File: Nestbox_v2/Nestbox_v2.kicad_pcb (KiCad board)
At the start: 2 copper layers, 85 x 60 mm, 116 parts, among them CON301 Micro_SD_Card, J201 BATT_CONN_01X02, J401 LB_DETECT_CONN_01X04, J402 CONN_01X05, J501 CONN_01X01, J502 CONN_01X06, J601 LOAD_CELL_CONN_01X04, J701 RFID_CONN_01X05, P301 RX/TX, P302 TST/RST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

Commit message: second PCB for EM4095 and created fabrication files of main board and corrected holes locations
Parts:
- moved C201 189.3 mm to (73.7, -20.5)
- moved C202 189.3 mm to (-3.31, -22.5)
- moved C203 189.3 mm to (63.5, -40.5)
- moved C204 189.3 mm to (-3.31, -14.5)
- moved C205 189.3 mm to (66.7, -20.5)
- moved C206 189.3 mm to (59.5, -41.0)
- moved C207 189.3 mm to (61.5, -41.0)
- moved C208 189.3 mm to (67.0, -38.0)
- moved C209 189.3 mm to (68.0, -41.0)
- moved C210 189.3 mm to (73.0, -41.0)
- moved C301 189.3 mm to (55.0, -23.0)
- moved C302 189.3 mm to (58.2, -20.0)
- moved C303 189.3 mm to (58.2, -18.0)
- moved C304 189.3 mm to (55.5, -12.0)
- moved C305 189.3 mm to (55.5, -13.7)
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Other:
- board text added: "VDD DATA CLK SLEEP GND"
- board text removed: "VDD CLK DATA SLEEP GND"

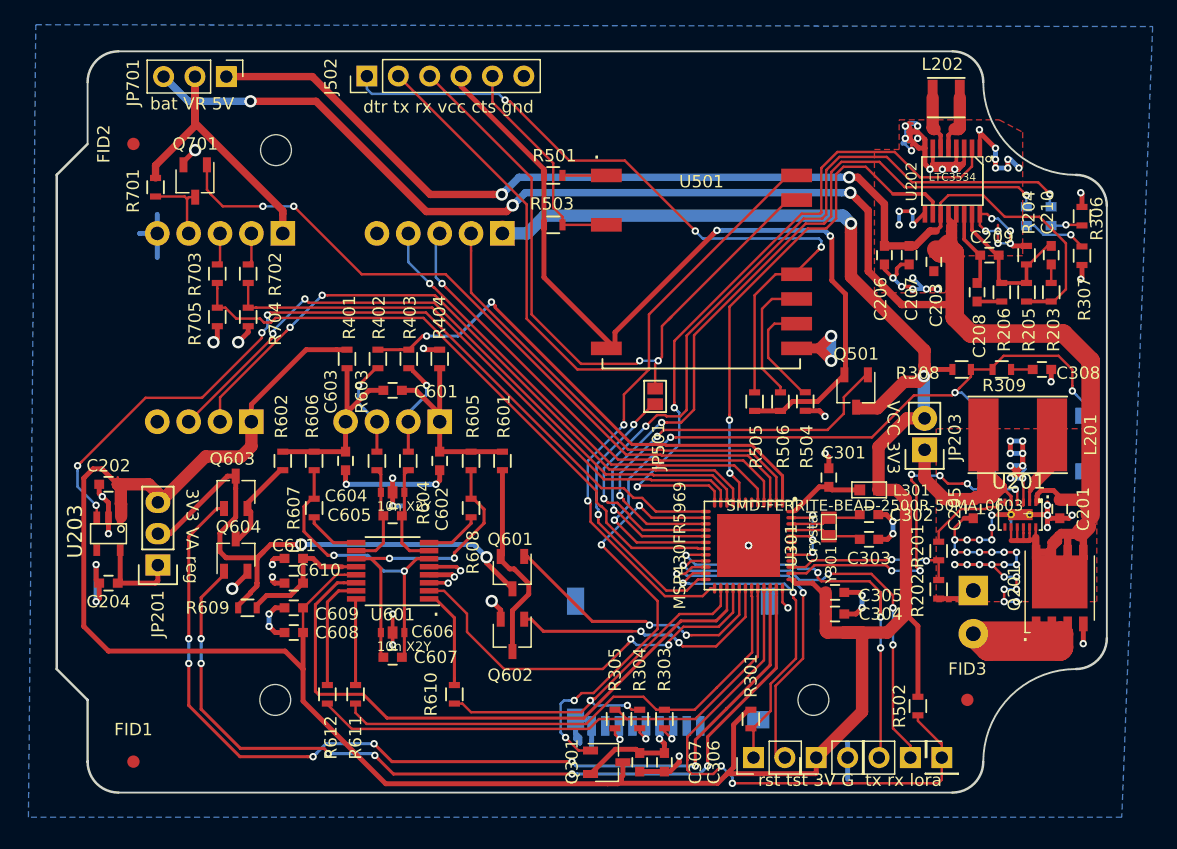
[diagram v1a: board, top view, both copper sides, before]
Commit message: TAPEOUT second batch nestbox main + EM pcb. added pull-ups, corrected pmos of load cell, WIFI AND SDCARD ENABLE PMOS ARE STILL WRONGLY ORIENTED
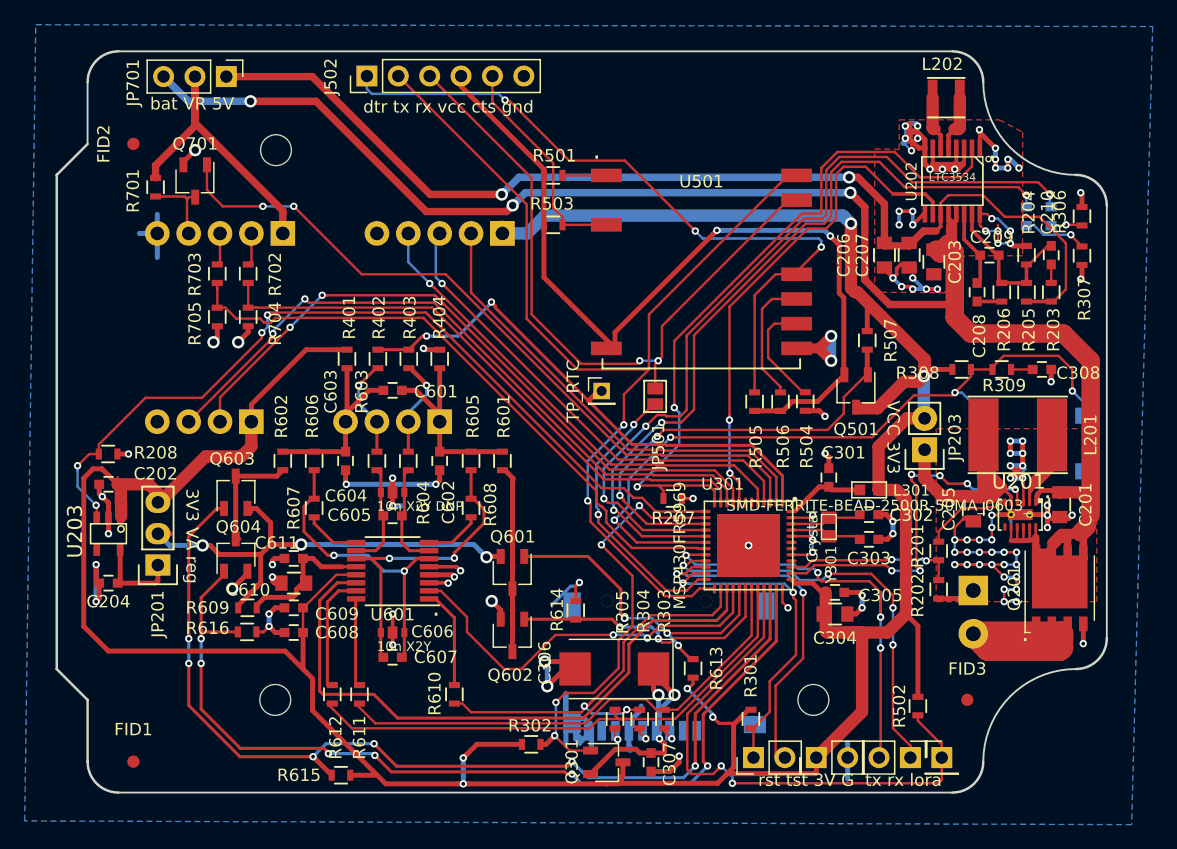
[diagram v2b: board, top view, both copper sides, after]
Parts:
- added R207: 82k, Resistors_SMD:R_0603, F.Cu at (42.4, -21.3)
- added R208: 82k, Resistors_SMD:R_0603, F.Cu at (-3.34, -24.9)
- added R302: 82k, Resistors_SMD:R_0603, F.Cu at (30.9, -1.41)
- added R507: 82k, Resistors_SMD:R_0603, F.Cu at (58.1, -34.1)
- added R613: 82k, Resistors_SMD:R_0603, F.Cu at (44.0, -7.55)
- added R614: 82k, Resistors_SMD:R_0603, F.Cu at (34.5, -12.3)
- added R615: 82k, Resistors_SMD:R_0603, F.Cu at (15.5, 1.09)
- added R616: 82k, Resistors_SMD:R_0603, F.Cu at (7.91, -10.5)
- added TP_RTC: CONN_01X01, Socket_Strips:Socket_Strip_Straight_1x01_Pitch2.00mm, F.Cu at (36.6, -30.0)
- C201, C203, C205, C206, C207, C304, C610: footprint Capacitors_SMD:C_0603 -> Capacitors_SMD:C_0805
- C306: footprint Capacitors_SMD:C_0603 -> Capacitors_Tantalum_SMD:CP_Tantalum_Case-D_EIA-7343-31_Reflow
- C604: value 10n X2Y -> 10n X2Y DNP
- C605: value 100n 1% -> 100n 1% DNP
- Q601: value DMG2301L-7 -> DMG2301L-7 -- Replace by 0R
- Q602, Q604: value DMG3402L -> DMG3402L DNP
- Q603: value DMG2301L-7 -> DMG2301L-7 DNP
- R502: value 10K -> 82k
- R601: value 1k 1% -> 1k 1% --> short with 0R
- R603: value 1k 1% -> 1k 1% --> short to 0R
- R604: value 1k 1% -> 1k 1% -- short to 0R
- R607, R608: value 0R -> 0R DNP
- moved C306 8.57 mm to (37.6, -7.50), turned to 180 degrees
- moved G*** 1.90 mm to (35.8, -31.0)
- moved C307 0.92 mm to (40.6, 0.04)
- moved CON301 0.49 mm to (42.1, -2.51)
- moved R612 0.40 mm to (14.8, -5.46)
- moved C201 0.35 mm to (73.7, -20.8)
- moved R611 0.32 mm to (17.0, -5.46)
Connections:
- Q601 pad 2: Net-(Q601-Pad2) -> VAA
- Q601 pad 3: VAA -> Net-(Q601-Pad3)
- Q602 pad 3: Net-(Q601-Pad2) -> Net-(Q601-Pad3)
- Q603 pad 2: Net-(Q603-Pad2) -> VAA
- Q603 pad 3: VAA -> Net-(Q603-Pad3)
- Q604 pad 3: Net-(Q603-Pad2) -> Net-(Q603-Pad3)
- R601 pad 2: Net-(Q601-Pad2) -> Net-(Q601-Pad3)
- R602 pad 2: Net-(Q603-Pad2) -> Net-(Q603-Pad3)
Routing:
- net GND: track 223.1 -> 249.3 mm, vias 109 -> 114
- net +3V3: track 244.9 -> 265.8 mm, vias 2 -> 6
- net Net-(Q601-Pad2): track 16.4 -> 0.00 mm
- net Net-(Q601-Pad3): track 0.00 -> 15.2 mm
- net Net-(C306-Pad1): track 9.30 -> 21.0 mm, vias 1 -> 3
- net Net-(Q603-Pad3): track 0.00 -> 9.54 mm
- net Net-(Q603-Pad2): track 7.63 -> 0.00 mm
- net VAA: track 47.3 -> 41.7 mm, vias 2 -> 3
- net /Load_Cell/EXC_A_P: track 22.9 -> 27.0 mm, vias 2 -> 3
- net /Load_Cell/EXC_B_N: track 72.1 -> 76.0 mm
- net /Load_Cell/EXC_B_P: track 78.5 -> 81.8 mm
- net /Control/SPI_CLK: track 31.6 -> 34.2 mm
- net Net-(CON301-Pad7): track 3.20 -> 1.13 mm
- net /Communication/ESP12_ENABLE: track 33.9 -> 35.9 mm
- net /Control/SPI_MOSI: track 41.7 -> 40.2 mm
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
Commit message: various annotations and changes
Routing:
- net Net-(C306-Pad1): track 21.0 -> 19.0 mm
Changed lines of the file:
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@@
   (general
     (links 277)
-    (no_connects 0)
+    (no_connects 1)
     (area -80.29 -82.95 95.35 8.700001)
     (thickness 1.6)
     (drawings 64)
-    (tracks 1751)
+    (tracks 1752)
     (zones 0)
     (modules 125)
@@
   (segment (start 51.975 -18.75) (end 54.5007 -18.75) (width 0.2) (layer F.Cu) (net 7))
   (segment (start 54.5007 -18.75) (end 55 -18.2507) (width 0.2) (layer F.Cu) (net 7))
+  (segment (start 40.71 -0.805) (end 41.11 -1.205) (width 0.4) (layer F.Cu) (net 8))
+  (segment (start 41.11 -1.205) (end 41.11 -1.675) (width 0.4) (layer F.Cu) (net 8))
+  (segment (start 41.11 -1.675) (end 41.29 -1.855) (width 0.4) (layer F.Cu) (net 8))
+  (segment (start 40.61 -0.705) (end 40.71 -0.805) (width 0.2) (layer F.Cu) (net 8))
+  (segment (start 35.71 0.995) (end 37.71 -1.005) (width 0.4) (layer F.Cu) (net 8))
+  (segment (start 37.71 -1.005) (end 39.39 -1.005) (width 0.4) (layer F.Cu) (net 8))
+  (segment (start 39.39 -1.005) (end 39.59 -0.805) (width 0.4) (layer F.Cu) (net 8))
+  (segment (start 39.59 -0.805) (end 40.71 -0.805) (width 0.4) (layer F.Cu) (net 8))
   (segment (start 42.51 -5.405) (end 41.29958 -4.19458) (width 0.4) (layer B.Cu) (net 8))
   (segment (start 41.29958 -4.19458) (end 41.29958 -2.90096) (width 0.4) (layer B.Cu) (net 8))
@@
   (segment (start 40.81 -5.805) (end 41.21 -5.405) (width 0.4) (layer F.Cu) (net 8))
   (via (at 41.21 -5.405) (size 1) (drill 0.6) (layers F.Cu B.Cu) (net 8))
-  (segment (start 40.61 -0.705) (end 41.69 -0.705) (width 0.2) (layer F.Cu) (net 8))
-  (segment (start 35.71 0.995) (end 37.71 -1.005) (width 0.4) (layer F.Cu) (net 8))
-  (segment (start 37.71 -1.005) (end 39.39 -1.005) (width 0.4) (layer F.Cu) (net 8))
-  (segment (start 39.39 -1.005) (end 39.69 -0.705) (width 0.4) (layer F.Cu) (net 8))
   (segment (start 41.29 -1.855) (end 41.29 -2.89138) (width 0.4) (layer B.Cu) (net 8))
   (segment (start 41.29 -2.89138) (end 41.29958 -2.90096) (width 0.4) (layer B.Cu) (net 8))
-  (segment (start 41.69 -0.705) (end 41.69 -1.455) (width 0.4) (layer F.Cu) (net 8))
-  (segment (start 41.69 -1.455) (end 41.29 -1.855) (width 0.4) (layer F.Cu) (net 8))
   (via (at 41.29 -1.855) (size 0.6) (drill 0.3) (layers F.Cu B.Cu) (net 8))
-  (segment (start 39.69 -0.705) (end 41.69 -0.705) (width 0.4) (layer F.Cu) (net 8))
   (segment (start 69.75 -31.75) (end 71.5 -31.75) (width 0.2) (layer F.Cu) (net 9))
   (segment (start 23.5 -28.145) (end 23.5 -27.52) (width 0.4) (layer F.Cu) (net 10))
